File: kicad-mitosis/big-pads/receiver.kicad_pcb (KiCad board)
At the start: 2 copper layers, 38.1 x 18 mm, 10 parts, among them P1 Header, 6-Pin, P2 Header, 6-Pin, P3 Header, 4-Pin, U1 NRF51822 (B)

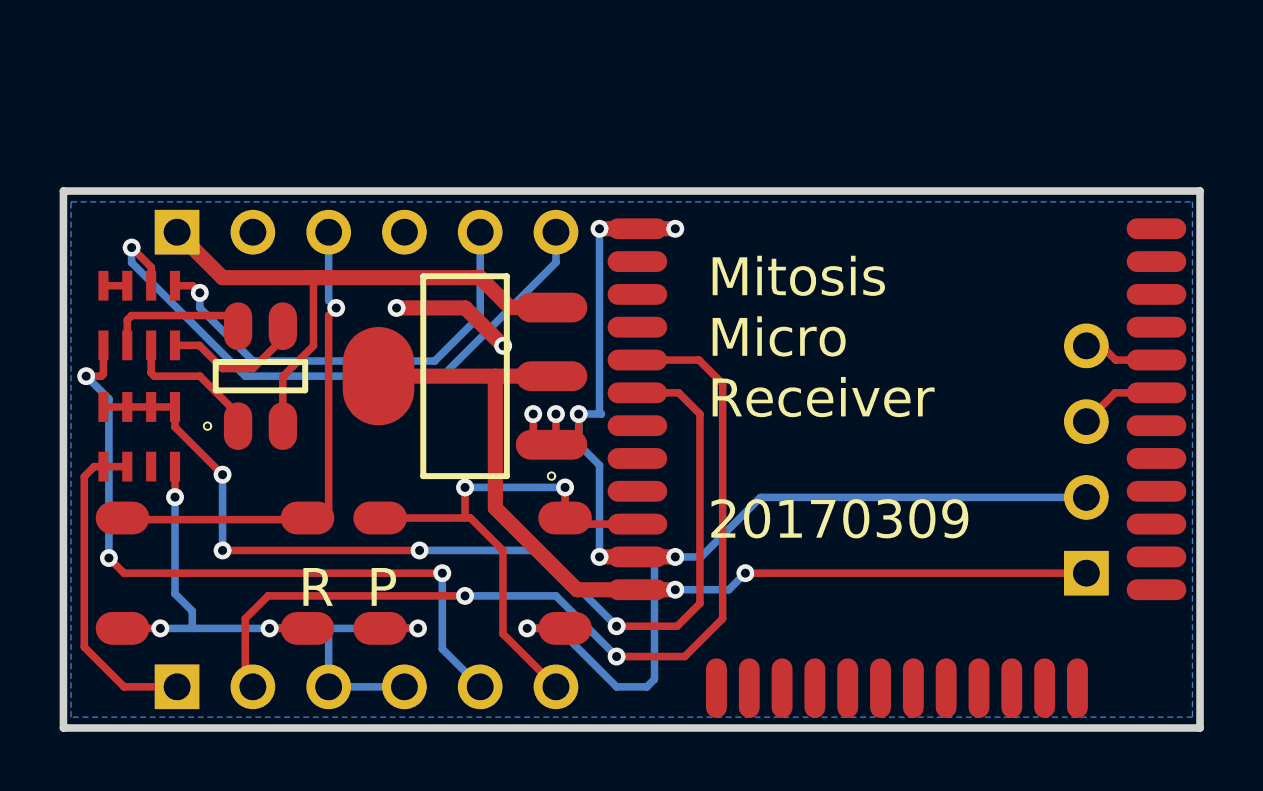
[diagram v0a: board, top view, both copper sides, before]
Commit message: modify big pad
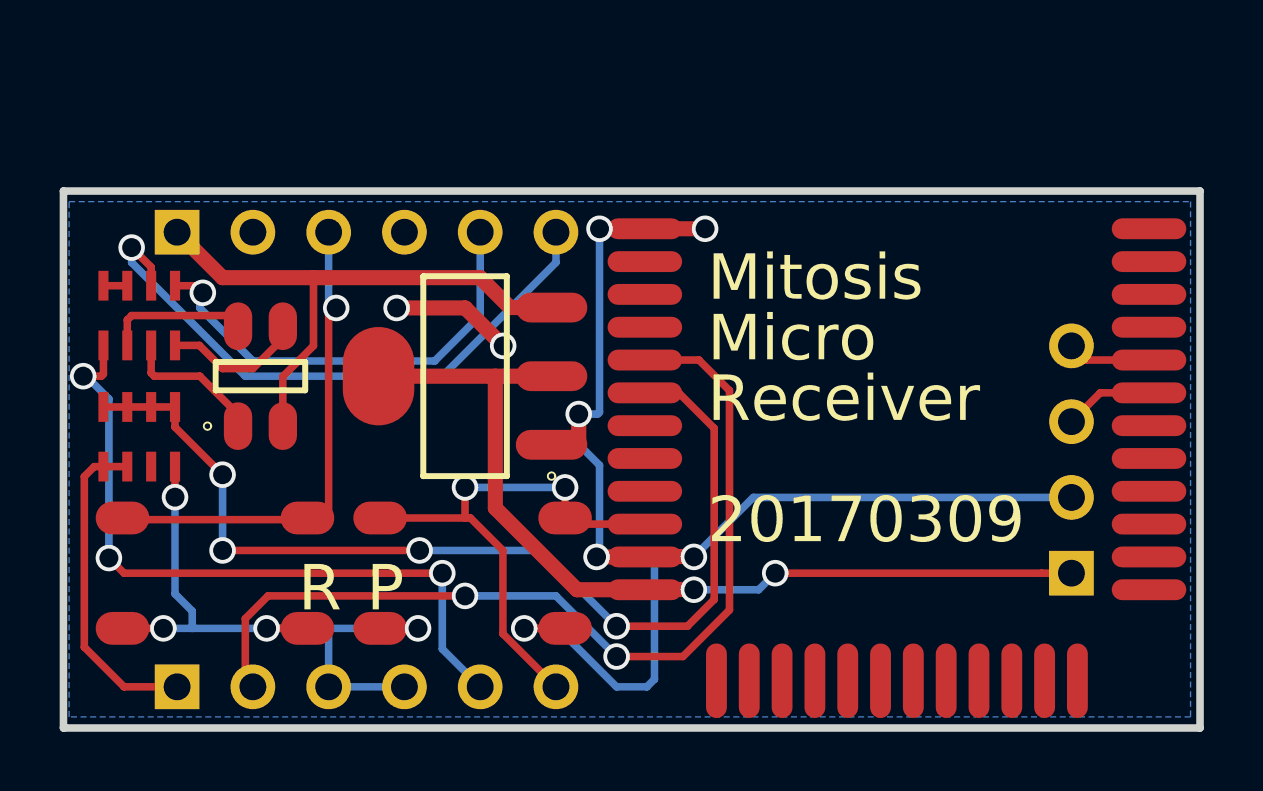
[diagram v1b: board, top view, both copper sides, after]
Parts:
- U1: footprint Core51822 (B) -> RF_Module:Core51822 (B)_big
- moved P3 0.50 mm to (96.7, -74.9)
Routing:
- net (no net): track 37.7 -> 33.6 mm, vias 2 -> 0
- net GND: track 69.2 -> 70.6 mm
- net VCC: track 31.4 -> 30.3 mm
- net TXO_DIV: track 34.0 -> 34.6 mm

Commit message: Modify receiver pcb to use black nrf
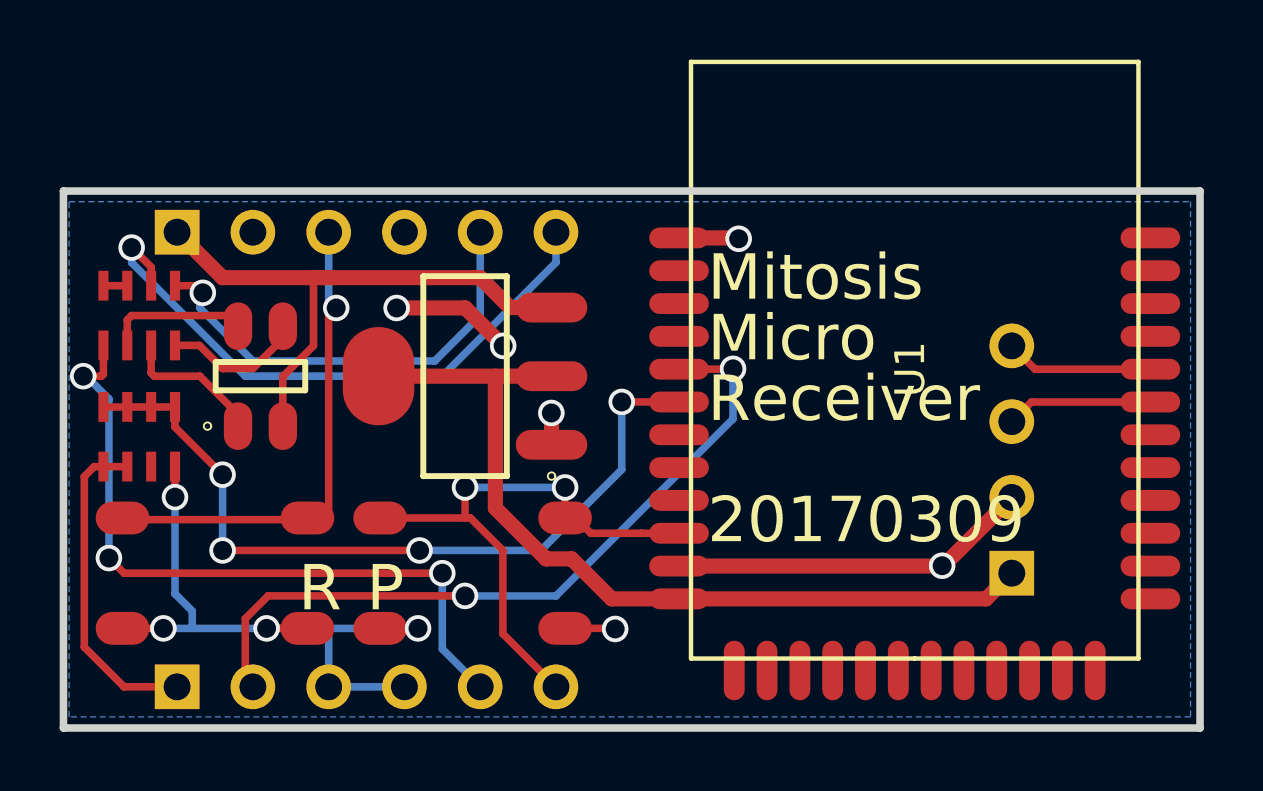
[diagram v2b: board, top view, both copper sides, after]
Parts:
- U1: footprint RF_Module:Core51822 (B)_big -> Atreus_Split:CORE_NRF51822_Black_core_pin
- moved U1 10.3 mm to (91.2, -81.8)
- moved P3 2.00 mm to (94.7, -74.9)
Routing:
- net GND: track 70.6 -> 43.6 mm, vias 12 -> 10
- net TXO_DIV: track 34.6 -> 26.6 mm
- net RXI: track 31.3 -> 25.0 mm
- net SWCLK: track 2.80 -> 4.97 mm
- net SWDIO: track 3.00 -> 4.92 mm
- net P-D3: track 17.8 -> 19.6 mm
- net VCC: track 30.3 -> 29.2 mm, vias 2 -> 0
